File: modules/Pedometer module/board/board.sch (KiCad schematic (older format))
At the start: 28 parts, among them J1 USB_C_Receptacle, J2 Conn_02x12_Odd_Even, J3 Conn_01x06_Female, Q1 AO3400A, SW1 SW_Push, SW2 SW_Push, U1 HT7833, U2 ESP32-WROOM-32D

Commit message: Pedometer module: Schematic and PCB layout
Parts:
- removed C1, C3: 1nF, Capacitor_SMD:C_0805_2012Metric_Pad1.18x1.45mm_HandSolder, symbol Device:C_Small
- removed D2: LED_RGBC, LED_THT:LED_D5.0mm-4_RGB, symbol Device:LED_RGBC
- removed J1: USB_C_Receptacle, Connector_USB:USB_C_Receptacle_JAE_DX07S024WJ1R350, symbol Connector:USB_C_Receptacle
- removed J2: Conn_02x12_Odd_Even, Connector_PinSocket_2.54mm:PinSocket_2x12_P2.54mm_Vertical_SMD, symbol Connector_Generic:Conn_02x12_Odd_Even
- removed U1: HT7833, Package_TO_SOT_SMD:SOT-89-3, symbol Regulator_Linear:HT75xx-1-SOT89
- added D2: LED_RGB, LED_SMD:LED_RGB_5050-6, symbol Device:LED_RGB
- added J1: USB_C_Receptacle_USB2.0, Connector_USB:USB_C_Receptacle_HRO_TYPE-C-31-M-12, symbol Connector:USB_C_Receptacle_USB2.0
- added J2, J3: Conn_01x06_Female, Board:SolderWire_1x06_P2.54mm, symbol Connector:Conn_01x06_Female
- added R7: 100R, Resistor_SMD:R_0805_2012Metric_Pad1.20x1.40mm_HandSolder, symbol Device:R_Small_US
- added R8: 10k, Resistor_SMD:R_0805_2012Metric_Pad1.20x1.40mm_HandSolder, symbol Device:R_Small_US
- added SW3: SW_SPST, Board:SW-SPDT-PCM12, symbol Switch:SW_SPST
- added U1: ME6211, Package_TO_SOT_SMD:SOT-23-5_HandSoldering, symbol ME6211:ME6211
- C1: renamed from C2; value 1uF -> 10uF
- C2: renamed from C4; value 2.2uF -> 10uF
- H1, H2: footprint MountingHole:MountingHole_3.2mm_M3 -> MountingHole:MountingHole_2.2mm_M2
- H3, H4: footprint MountingHole:MountingHole_3.2mm_M3 -> MountingHole:MountingHole_2.5mm
- SW1, SW2: footprint Button_Switch_SMD:SW_SPST_Omron_B3FS-100xP -> Button_Switch_SMD:SW_SPST_B3U-1000P
- renumbered J3 to J4, R18 to R10, R19 to R11, R7 to R9
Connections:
- wire segments 123 -> 116
- no-connect marks 26 -> 18
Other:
- moved on the sheet: BZ1, C1, C2, D1, H1, H2, H3, H4, J4, Q1, R1, R10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

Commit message: Pedometer module: PCB size reduced
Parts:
- added D2: LED, LED_SMD:LED_0805_2012Metric_Pad1.15x1.40mm_HandSolder, symbol Device:LED
- added R5: 12k, Resistor_SMD:R_0805_2012Metric_Pad1.20x1.40mm_HandSolder, symbol Device:R_Small_US
- J4: footprint Connector_PinSocket_2.54mm:PinSocket_1x06_P2.54mm_Vertical -> Board:SolderWire_1x06_P2.54mm
- renumbered D2 to D3, R9 to R10, R10 to R11, R11 to R12, R5 to R6, R6 to R7, R7 to R8, R8 to R9
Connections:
- net GND: now also D2.1 (K)
- net IO15: now also R5.1
- new net: D2.2 (A), R5.2
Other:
- moved on the sheet: D1, J2, J3, R1, R10, R6, R7, SW1, SW2

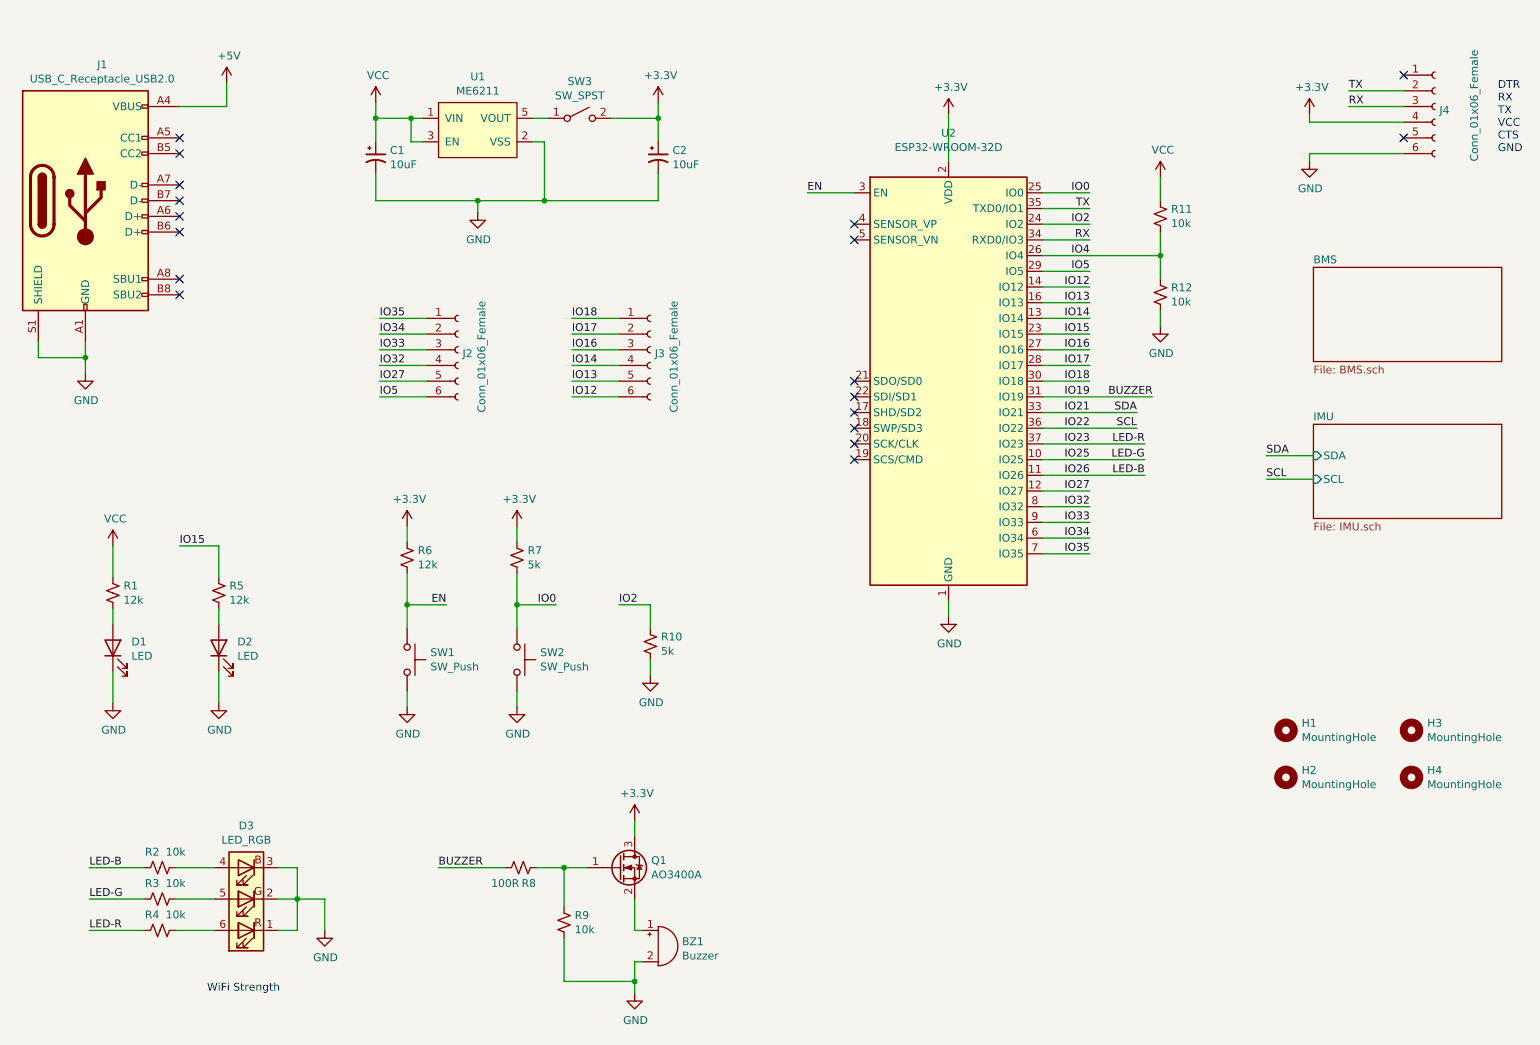
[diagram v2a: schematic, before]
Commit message: Pedometer module: PCB complete
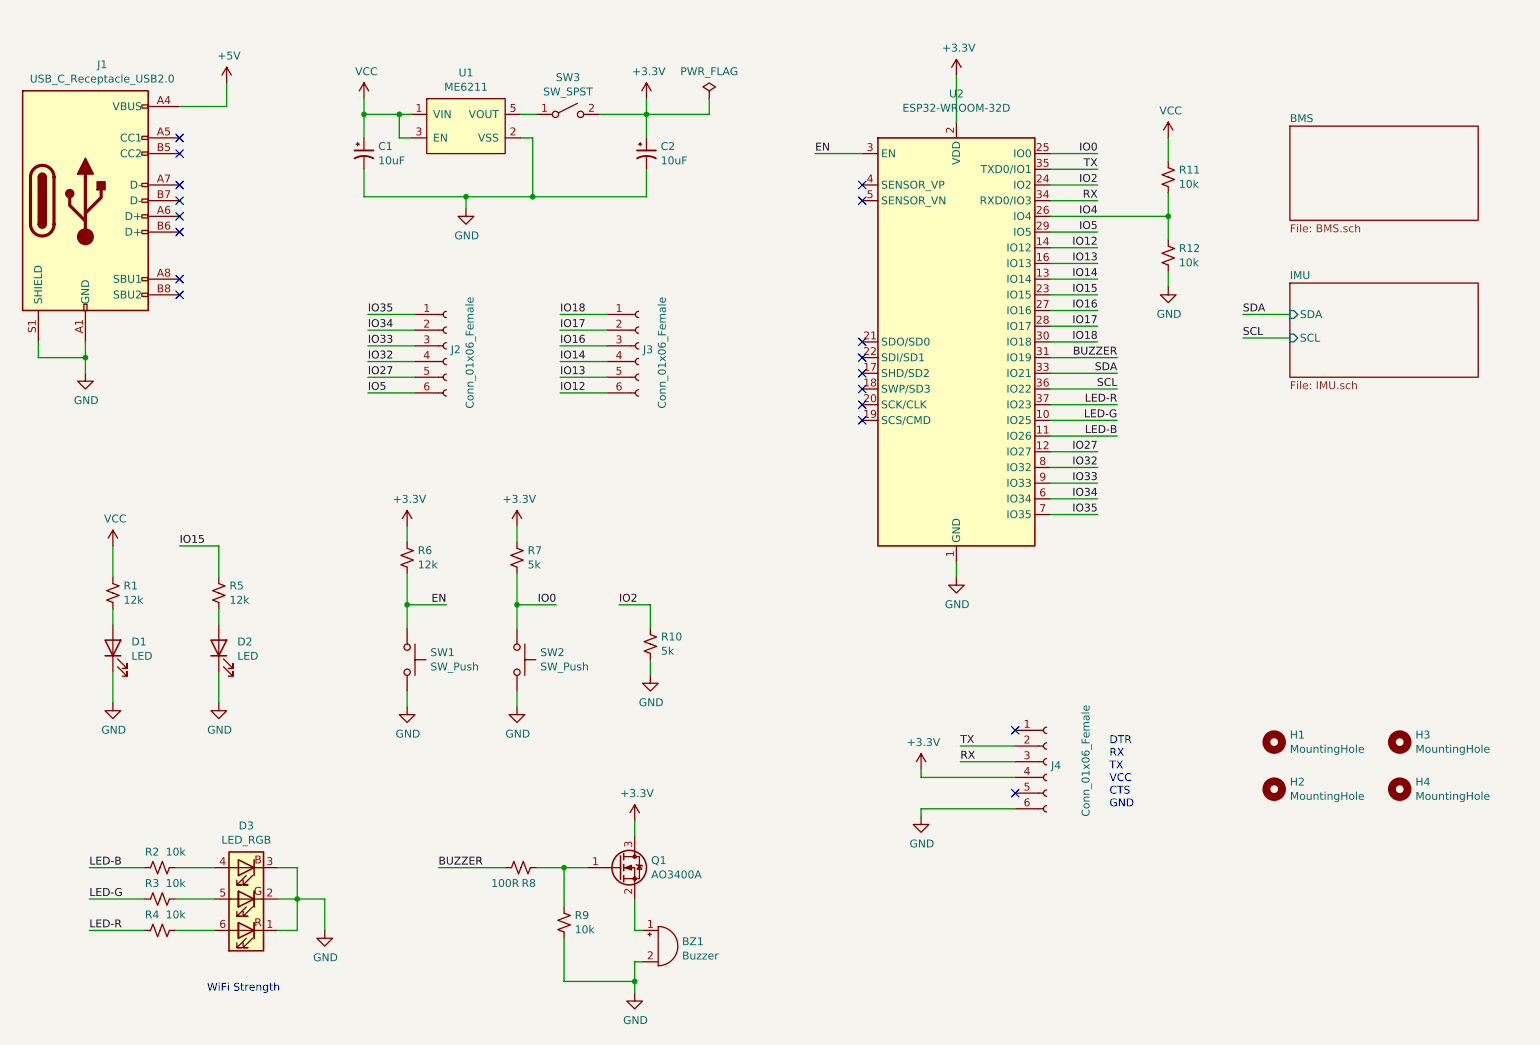
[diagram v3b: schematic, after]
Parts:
- U2: footprint RF_Module:ESP32-WROOM-32 -> Board:ESP32-WROOM-32
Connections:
- net IO21 renamed SDA
- net IO22 renamed SCL
- net IO23 renamed LED-R
- net IO25 renamed LED-G
- net IO26 renamed LED-B
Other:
- moved on the sheet: C1, C2, H1, H2, H3, H4, J2, J3, J4, R11, R12, SW3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

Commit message: Pedometer module: PCB modular
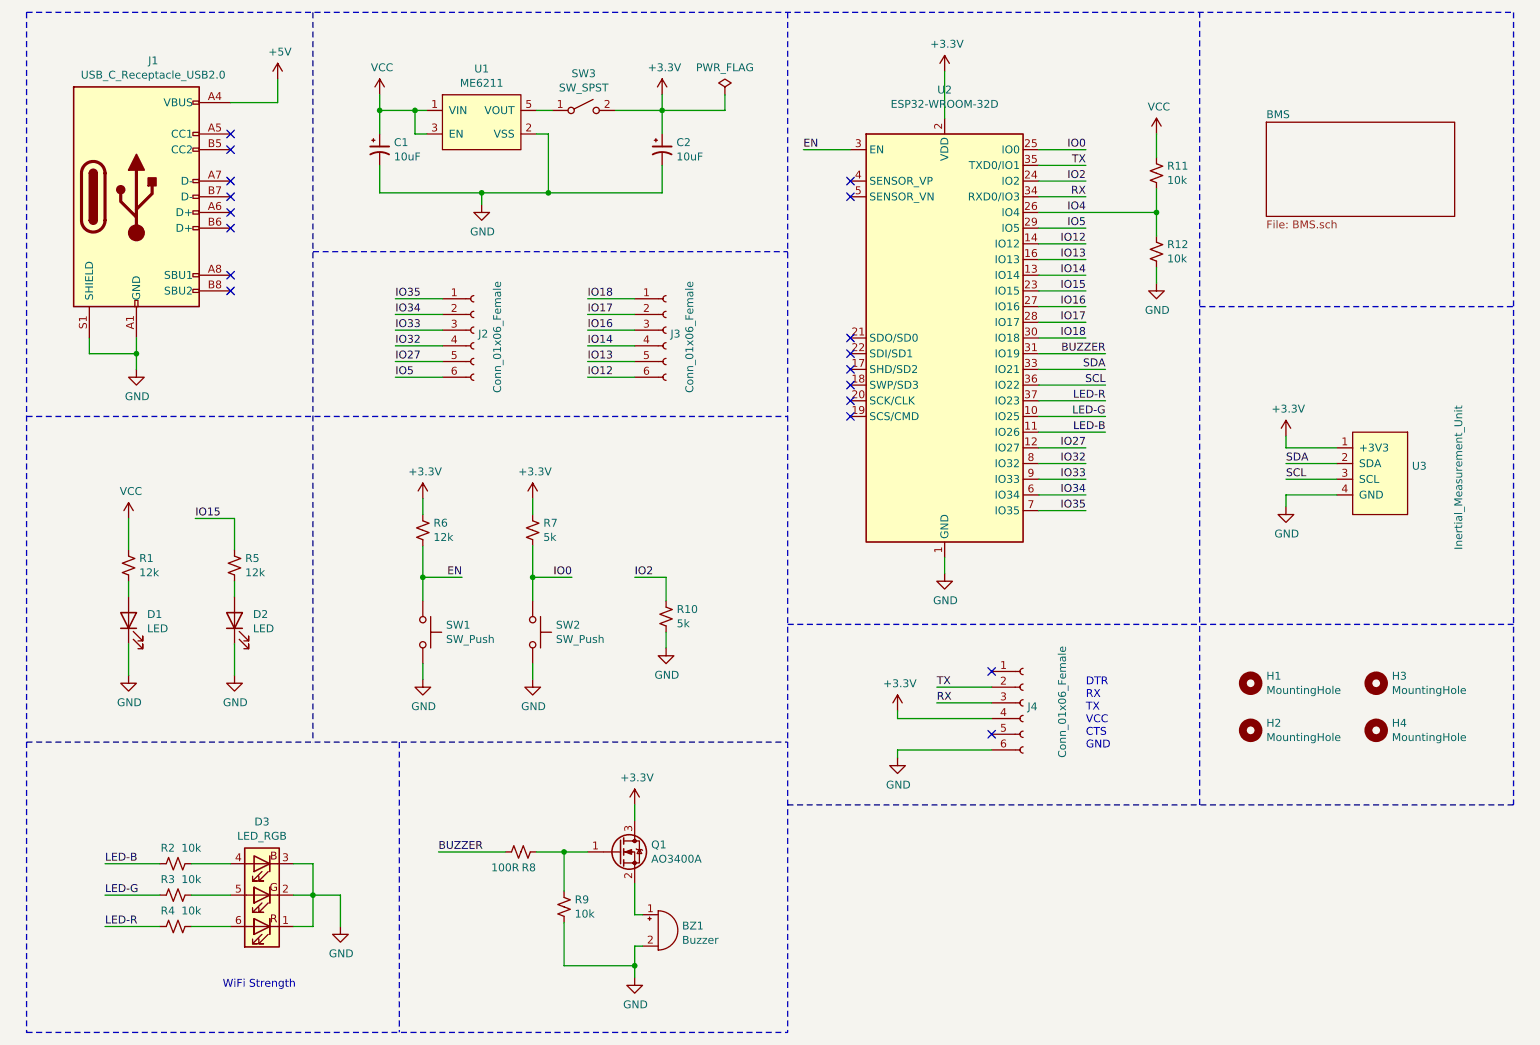
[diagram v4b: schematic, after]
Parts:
- added U3: Inertial_Measurement_Unit, Board:Inertial_Measurement_Unit_Board, symbol Board:Inertial_Measurement_Unit
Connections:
- net +3V3: now also U3.1 (+3V3)
- net GND: now also U3.4 (GND)
- net SCL: now also U3.3 (SCL)
- net SDA: now also U3.2 (SDA)
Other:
- moved on the sheet: BZ1, C1, C2, D1, D2, D3, H1, H2, H3, H4, J1, J2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

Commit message: PCB: IMU
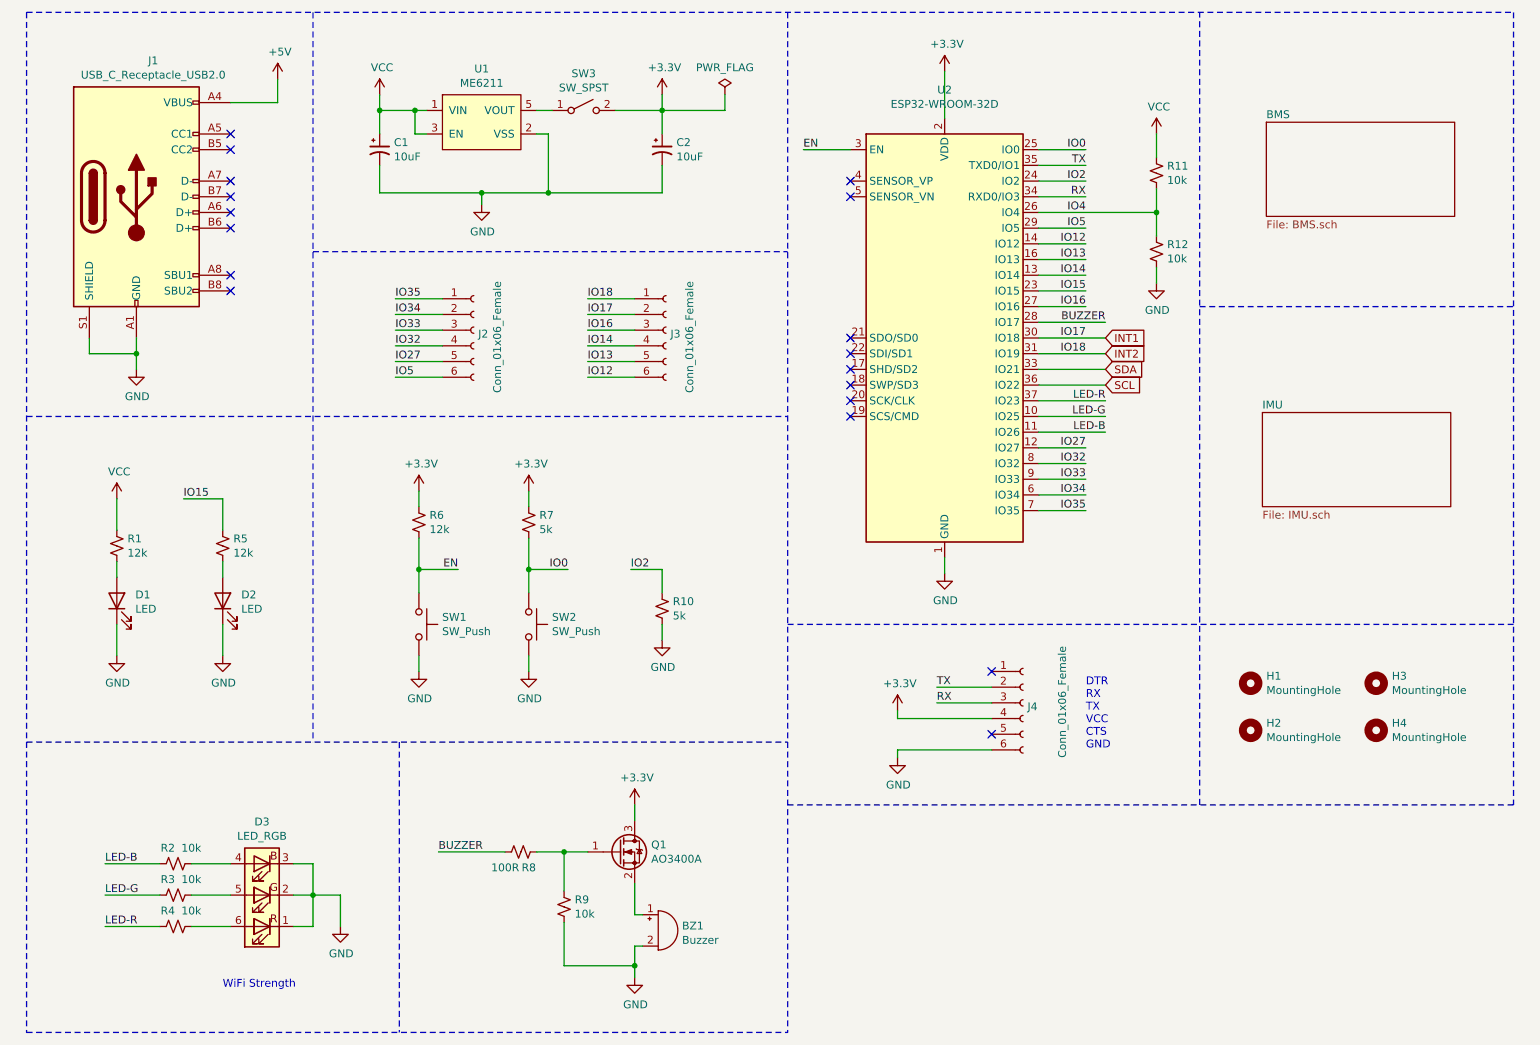
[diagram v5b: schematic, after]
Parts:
- removed U3: Inertial_Measurement_Unit, Board:Inertial_Measurement_Unit_Board, symbol Board:Inertial_Measurement_Unit
- J1: footprint Connector_USB:USB_C_Receptacle_HRO_TYPE-C-31-M-12 -> Board:USB_C_Receptacle_HRO_TYPE-C-31-M-12
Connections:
- net BUZZER: now also U2.28 (IO17); no longer U2.31 (IO19)
- net IO17 renamed INT1
- net INT1: now also U2.30 (IO18); no longer U2.28 (IO17)
- net IO18 renamed INT2
- net INT2: now also U2.31 (IO19); no longer U2.30 (IO18)
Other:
- moved on the sheet: D1, D2, R1, R10, R5, R6, R7, SW1, SW2
